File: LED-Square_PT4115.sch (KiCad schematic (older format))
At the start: 23 parts, among them P1 IN, P2 OUT, U1 PT4115-SOT89-5

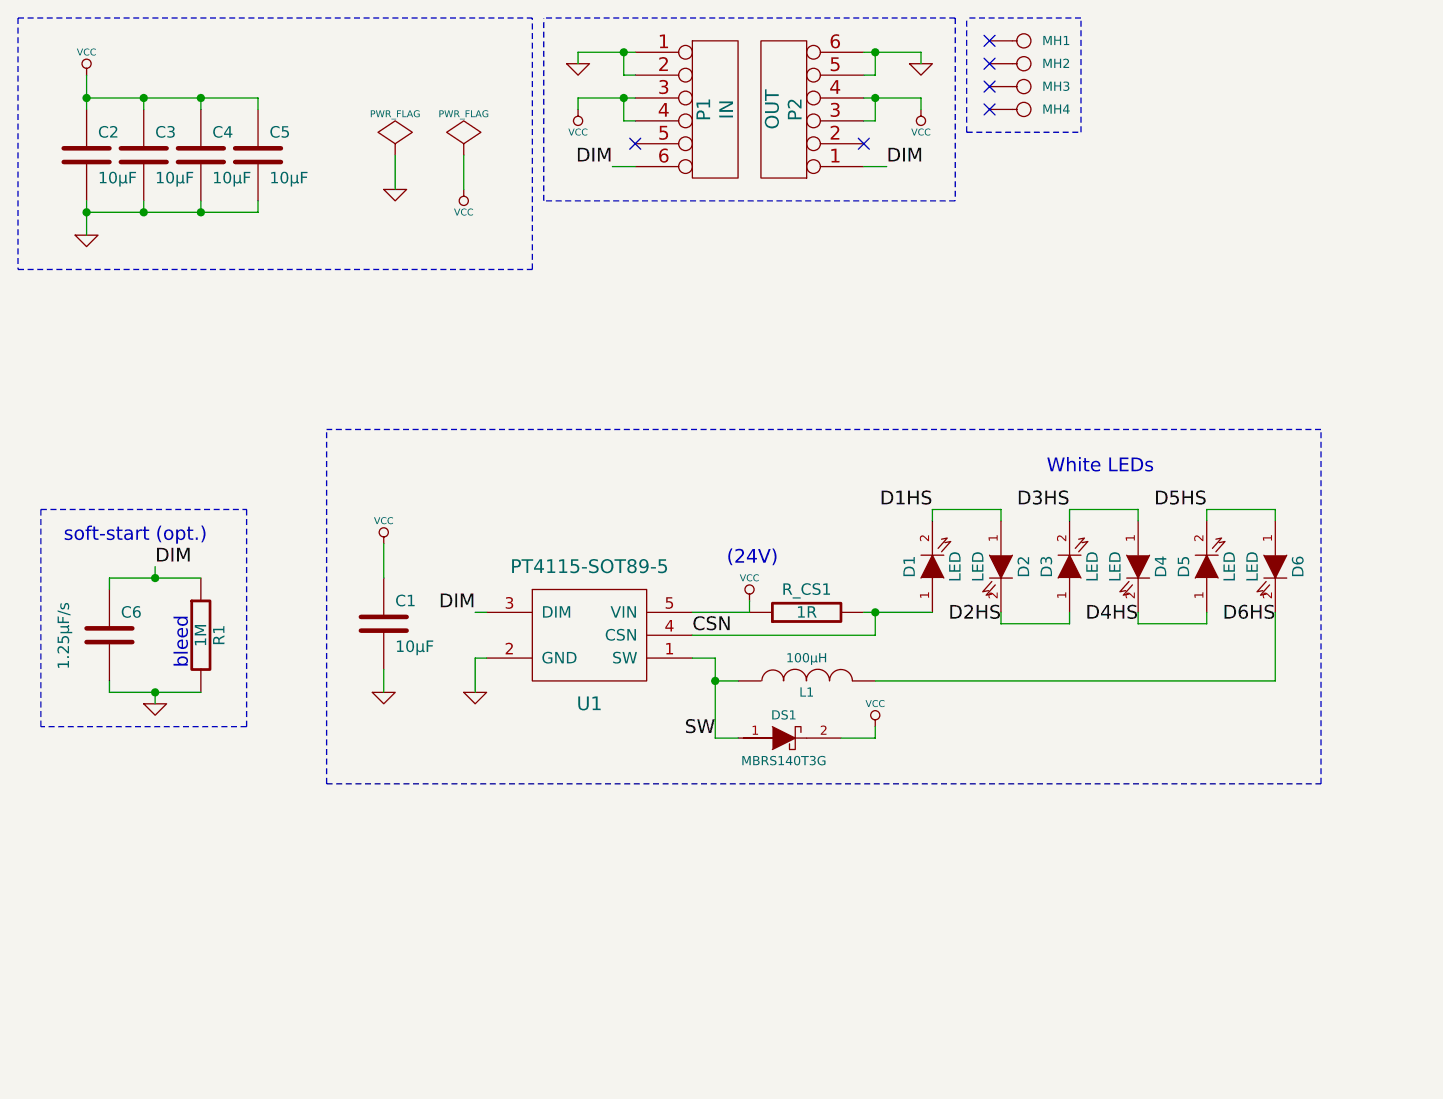
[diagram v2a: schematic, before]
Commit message: Added a 5.6V Zener to protect the PT4115's DIM input. It badly needs it.
Upped schematic + pcb revision to V0.2
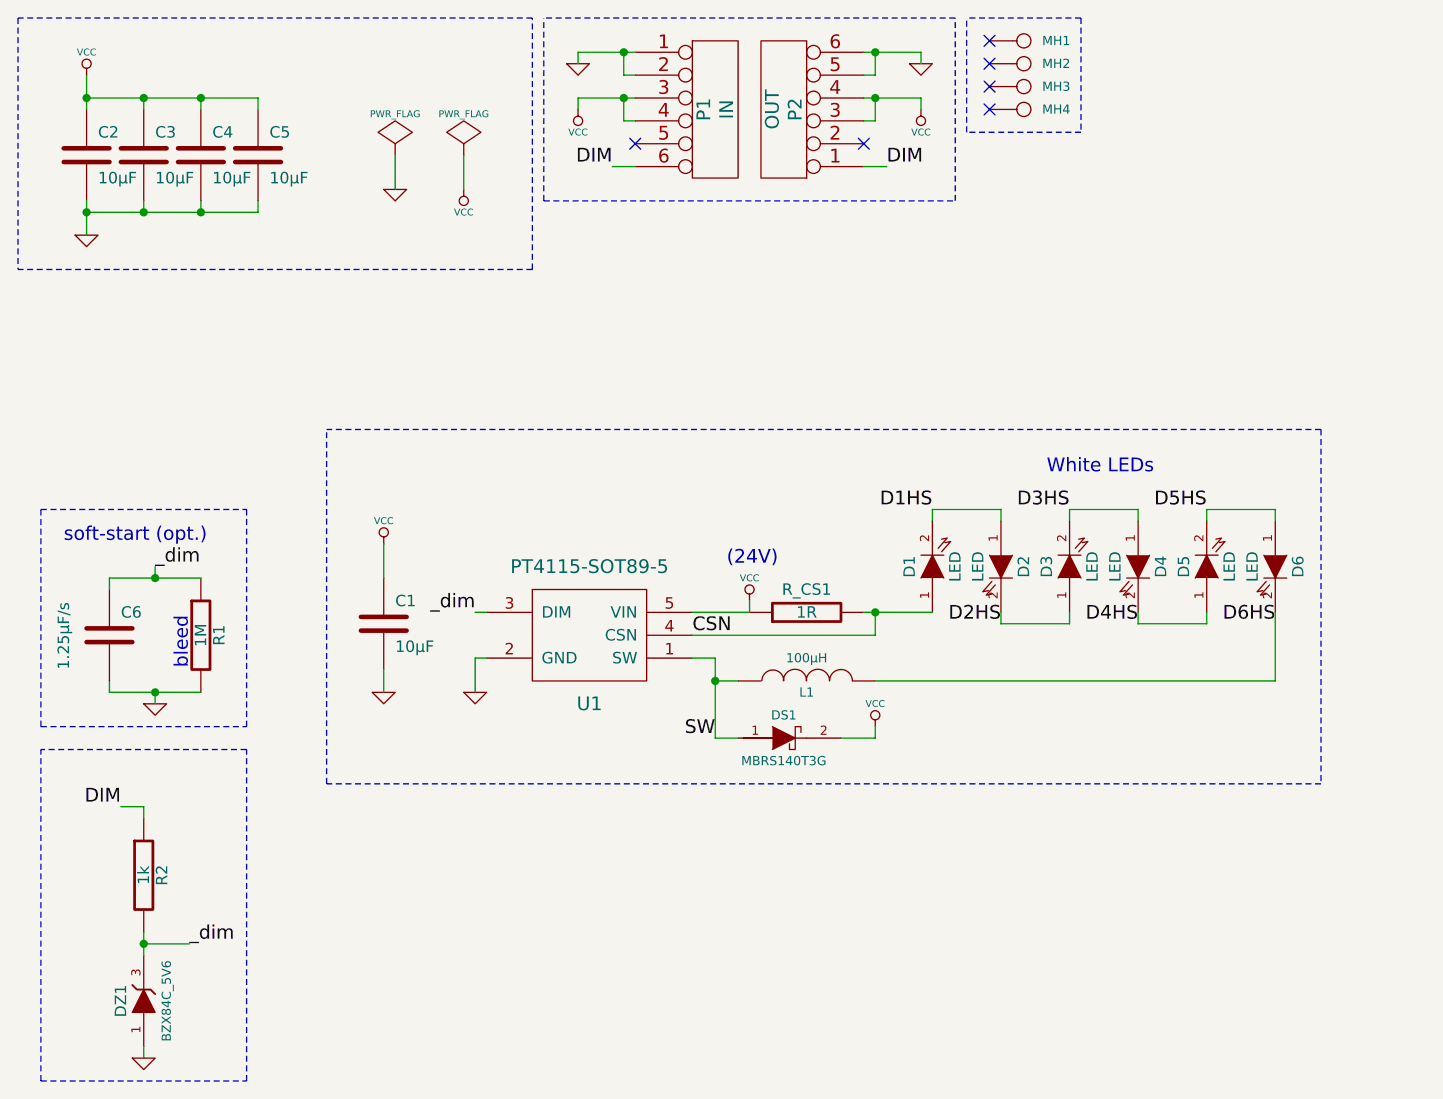
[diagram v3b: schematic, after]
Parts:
- added DZ1: BZX84C_5V6, symbol MADW__ZENER_SOT23
- added R2: 1k, symbol R
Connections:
- net DIM: now also R2.1; no longer C6.1, R1.1, U1.3 (DIM)
- net GND: now also DZ1.1
- new net _dim: C6.1, DZ1.3, R1.1, R2.2, U1.3 (DIM)
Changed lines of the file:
@@
-EESchema Schematic File Version 2  date Sun 11 Nov 2012 12:08:53 AM CET
+EESchema Schematic File Version 2  date Sun 11 Nov 2012 09:42:30 PM CET
 LIBS:my_parts
 LIBS:power
@@
 EELAYER 25  0
 EELAYER END
-$Descr User 8266 5866
+$Descr User 8265 5866
 encoding utf-8
 Sheet 1 1
 Title "LED-Square PT4115"
-Date "10 nov 2012"
-Rev "0.10"
+Date "11 nov 2012"
+Rev "0.20"
 Comp "2012 - blog.spitzenpfeil.org"
 Comment1 ""
@@
 Comment4 ""
 $EndDescr
+$Comp
+L MADW__ZENER_SOT23 DZ1
+U 1 1 50A00A38
+P 1100 4850
+F 0 "DZ1" H 1100 4950 50  0000 C CNN
+F 1 "BZX84C_5V6" H 1100 4750 40  0000 C CNN
+	1    1100 4850
+	0    -1   -1   0
+$EndComp
+Wire Wire Line
+	1100 4600 1300 4600
+Wire Wire Line
+	1000 4000 1100 4000
+Wire Wire Line
+	1100 4000 1100 4050
+Connection ~ 1150 3500
+Wire Wire Line
+	1150 3550 1150 3500
+Wire Notes Line
+	650  2700 1550 2700
+Wire Wire Line
+	950  3450 950  3500
+Wire Wire Line
+	950  3050 950  3000
+Wire Notes Line
+	6250 2350 1900 2350
+Wire Notes Line
+	6250 2350 6250 3900
+Wire Notes Line
+	6250 3900 1900 3900
+Wire Notes Line
+	1900 3900 1900 2350
+Wire Notes Line
+	2800 1650 2800 550
+Wire Notes Line
+	2800 1650 550  1650
+Wire Notes Line
+	2800 550  550  550
+Connection ~ 850  1400
+Wire Wire Line
+	850  1500 850  1350
+Connection ~ 1350 1400
+Wire Wire Line
+	1350 1350 1350 1400
+Connection ~ 1100 900
+Wire Wire Line
+	1100 950  1100 900
+Wire Wire Line
+	1600 950  1600 900
+Wire Wire Line
+	1600 900  850  900
+Wire Wire Line
+	4500 750  4500 700
+Wire Wire Line
+	4500 700  4250 700
+Wire Wire Line
+	4500 950  4500 900
+Wire Wire Line
+	4500 900  4250 900
+Wire Wire Line
+	2550 3150 2600 3150
+Wire Wire Line
+	3250 900  3000 900
+Wire Wire Line
+	3000 900  3000 950
+Wire Wire Line
+	3250 700  3000 700
+Wire Wire Line
+	3000 700  3000 750
+Wire Wire Line
+	2200 1150 2200 1300
+Wire Wire Line
+	4300 3650 4300 3700
+Wire Wire Line
+	4300 3700 4150 3700
+Wire Wire Line
+	3600 3450 3700 3450
+Wire Wire Line
+	3500 3350 3600 3350
+Wire Wire Line
+	2150 3400 2150 3500
+Wire Wire Line
+	4300 3150 4300 3250
+Wire Wire Line
+	4300 3250 3500 3250
+Wire Wire Line
+	2550 3500 2550 3350
+Wire Wire Line
+	2550 3350 2600 3350
+Wire Wire Line
+	5750 3150 5750 3200
+Wire Wire Line
+	5750 3200 5450 3200
+Wire Wire Line
+	5450 3200 5450 3150
+Wire Wire Line
+	5150 3150 5150 3200
+Wire Wire Line
+	5150 3200 4850 3200
+Wire Wire Line
+	4850 3200 4850 3150
+Wire Wire Line
+	4550 2750 4550 2700
+Wire Wire Line
+	4550 2700 4850 2700
+Wire Wire Line
+	4850 2700 4850 2750
+Wire Wire Line
+	5150 2750 5150 2700
+Wire Wire Line
+	5150 2700 5450 2700
+Wire Wire Line
+	5450 2700 5450 2750
+Wire Wire Line
+	5750 2750 5750 2700
+Wire Wire Line
+	5750 2700 6050 2700
+Wire Wire Line
+	6050 2700 6050 2750
+Wire Wire Line
+	3500 3150 3750 3150
+Wire Wire Line
+	3750 3150 3750 3100
+Wire Wire Line
+	2150 2850 2150 3000
+Wire Wire Line
+	4550 3150 4250 3150
+Connection ~ 4300 3150
+Wire Wire Line
+	4300 3450 6050 3450
+Wire Wire Line
+	6050 3450 6050 3150
+Wire Wire Line
+	3600 3350 3600 3700
+Wire Wire Line
+	3600 3700 3700 3700
+Connection ~ 3600 3450
+Wire Wire Line
+	2500 1150 2500 1300
+Wire Wire Line
+	3250 800  3200 800
+Wire Wire Line
+	3200 800  3200 700
+Connection ~ 3200 700
+Wire Wire Line
+	3200 900  3200 1000
+Connection ~ 3200 900
+Wire Wire Line
+	3200 1000 3250 1000
+Wire Wire Line
+	3150 1200 3250 1200
+Wire Wire Line
+	4250 1200 4350 1200
+Wire Wire Line
+	4250 1000 4300 1000
+Wire Wire Line
+	4300 1000 4300 900
+Connection ~ 4300 900
+Wire Wire Line
+	4250 800  4300 800
+Wire Wire Line
+	4300 800  4300 700
+Connection ~ 4300 700
+Wire Wire Line
+	1350 950  1350 900
+Connection ~ 1350 900
+Wire Wire Line
+	850  1400 1600 1400
+Wire Wire Line
+	1600 1400 1600 1350
+Wire Wire Line
+	1100 1350 1100 1400
+Connection ~ 1100 1400
+Wire Wire Line
+	850  800  850  950
+Connection ~ 850  900
+Wire Notes Line
+	2850 1350 2850 550
+Wire Notes Line
+	2850 1350 4650 1350
+Wire Notes Line
+	4650 1350 4650 550
+Wire Notes Line
+	4650 550  2850 550
+Wire Notes Line
+	5200 550  4700 550
+Wire Notes Line
+	5200 550  5200 1050
+Wire Notes Line
+	5200 1050 4700 1050
+Wire Notes Line
+	4700 1050 4700 550
+Wire Notes Line
+	550  550  550  1650
+Wire Notes Line
+	650  2700 650  3650
+Wire Notes Line
+	650  3650 1550 3650
+Wire Notes Line
+	1550 3650 1550 2700
+Wire Wire Line
+	950  3000 1350 3000
+Wire Wire Line
+	950  3500 1350 3500
+Wire Wire Line
+	1150 2950 1150 3000
+Connection ~ 1150 3000
+Wire Wire Line
+	1100 5050 1100 5100
+Wire Wire Line
+	1100 4550 1100 4650
+Connection ~ 1100 4600
+Wire Notes Line
+	650  5200 650  3750
+Wire Notes Line
+	650  5200 1550 5200
+Wire Notes Line
+	1550 5200 1550 3750
+Wire Notes Line
+	1550 3750 650  3750
+Text Label 1000 4000 2    60   ~ 0
+DIM
+Text Label 1300 4600 0    60   ~ 0
+_dim
+$Comp
+L GND #PWR?
+U 1 1 509FF5E9
+P 1100 5100
+F 0 "#PWR?" H 1100 5100 30  0001 C CNN
+F 1 "GND" H 1100 5030 30  0001 C CNN
+	1    1100 5100
+	1    0    0    -1
+$EndComp
+$Comp
+L R R2
+U 1 1 509FF5DB
+P 1100 4300
+F 0 "R2" V 1180 4300 50  0000 C CNN
+F 1 "1k" V 1100 4300 50  0000 C CNN
+	1    1100 4300
+	1    0    0    -1
+$EndComp
 Text Notes 1300 3400 1    60   ~ 0
 bleed
-Connection ~ 1150 3000
-Wire Wire Line
-	1150 2950 1150 3000
-Wire Wire Line
-	1350 3500 950  3500
-Wire Wire Line
-	1350 3000 950  3000
-Wire Notes Line
-	1550 3650 1550 2700
-Wire Notes Line
-	1550 3650 650  3650
-Wire Notes Line
-	650  3650 650  2700
-Wire Notes Line
-	550  550  550  1650
-Wire Notes Line
-	4700 1050 4700 550
-Wire Notes Line
-	4700 1050 5200 1050
-Wire Notes Line
-	5200 1050 5200 550
-Wire Notes Line
-	5200 550  4700 550
-Wire Notes Line
-	4650 550  2850 550
-Wire Notes Line
-	4650 550  4650 1350
-Wire Notes Line
-	4650 1350 2850 1350
-Wire Notes Line
-	2850 1350 2850 550
-Connection ~ 850  900
-Wire Wire Line
-	850  800  850  950
-Connection ~ 1100 1400
-Wire Wire Line
-	1100 1350 1100 1400
-Wire Wire Line
-	1600 1350 1600 1400
-Wire Wire Line
-	1600 1400 850  1400
-Connection ~ 1350 900
-Wire Wire Line
-	1350 950  1350 900
-Connection ~ 4300 700
-Wire Wire Line
-	4300 700  4300 800
-Wire Wire Line
-	4300 800  4250 800
-Connection ~ 4300 900
-Wire Wire Line
-	4300 900  4300 1000
-Wire Wire Line
-	4300 1000 4250 1000
-Wire Wire Line
-	4250 1200 4350 1200
-Wire Wire Line
-	3150 1200 3250 1200
-Wire Wire Line
-	3250 1000 3200 1000
-Connection ~ 3200 900
-Wire Wire Line
-	3200 1000 3200 900
-Connection ~ 3200 700
-Wire Wire Line
-	3200 700  3200 800
-Wire Wire Line
-	3200 800  3250 800
-Wire Wire Line
-	2500 1150 2500 1300
-Connection ~ 3600 3450
-Wire Wire Line
-	3700 3700 3600 3700
-Wire Wire Line
-	3600 3700 3600 3350
-Wire Wire Line
-	6050 3150 6050 3450
-Wire Wire Line
-	6050 3450 4300 3450
-Connection ~ 4300 3150
-Wire Wire Line
-	4550 3150 4250 3150
-Wire Wire Line
-	2150 2850 2150 3000
-Wire Wire Line
-	3750 3100 3750 3150
-Wire Wire Line
-	3750 3150 3500 3150
-Wire Wire Line
-	6050 2750 6050 2700
-Wire Wire Line
-	6050 2700 5750 2700
-Wire Wire Line
-	5750 2700 5750 2750
-Wire Wire Line
-	5450 2750 5450 2700
-Wire Wire Line
-	5450 2700 5150 2700
-Wire Wire Line
-	5150 2700 5150 2750
-Wire Wire Line
-	4850 2750 4850 2700
-Wire Wire Line
-	4850 2700 4550 2700
-Wire Wire Line
-	4550 2700 4550 2750
-Wire Wire Line
-	4850 3150 4850 3200
-Wire Wire Line
-	4850 3200 5150 3200
-Wire Wire Line
-	5150 3200 5150 3150
-Wire Wire Line
-	5450 3150 5450 3200
-Wire Wire Line
-	5450 3200 5750 3200
-Wire Wire Line
-	5750 3200 5750 3150
-Wire Wire Line
-	2600 3350 2550 3350
-Wire Wire Line
-	2550 3350 2550 3500
-Wire Wire Line
-	3500 3250 4300 3250
-Wire Wire Line
-	4300 3250 4300 3150
-Wire Wire Line
-	2150 3400 2150 3500
-Wire Wire Line
-	3600 3350 3500 3350
-Wire Wire Line
-	3600 3450 3700 3450
-Wire Wire Line
-	4150 3700 4300 3700
-Wire Wire Line
-	4300 3700 4300 3650
-Wire Wire Line
-	2200 1150 2200 1300
-Wire Wire Line
-	3000 750  3000 700
-Wire Wire Line
-	3000 700  3250 700
-Wire Wire Line
-	3000 950  3000 900
-Wire Wire Line
-	3000 900  3250 900
-Wire Wire Line
-	2550 3150 2600 3150
-Wire Wire Line
-	4250 900  4500 900
-Wire Wire Line
-	4500 900  4500 950
-Wire Wire Line
-	4250 700  4500 700
-Wire Wire Line
-	4500 700  4500 750
-Wire Wire Line
-	850  900  1600 900
-Wire Wire Line
-	1600 900  1600 950
-Wire Wire Line
-	1100 950  1100 900
-Connection ~ 1100 900
-Wire Wire Line
-	1350 1350 1350 1400
-Connection ~ 1350 1400
-Wire Wire Line
-	850  1500 850  1350
-Connection ~ 850  1400
-Wire Notes Line
-	550  550  2800 550
-Wire Notes Line
-	550  1650 2800 1650
-Wire Notes Line
-	2800 1650 2800 550
-Wire Notes Line
-	1900 3900 1900 2350
-Wire Notes Line
-	1900 3900 6250 3900
-Wire Notes Line
-	6250 3900 6250 2350
-Wire Notes Line
-	6250 2350 1900 2350
-Wire Wire Line
-	950  3000 950  3050
-Wire Wire Line
-	950  3500 950  3450
-Wire Notes Line
-	650  2700 1550 2700
-Wire Wire Line
-	1150 3550 1150 3500
-Connection ~ 1150 3500
 $Comp
 L R R1
@@
 $EndComp
 Text Label 1150 2950 0    60   ~ 0
-DIM
+_dim
 $Comp
 L GND #PWR01
@@
 DIM
 Text Label 2550 3150 2    60   ~ 0
-DIM
+_dim
 $Comp
 L VCC #PWR04
